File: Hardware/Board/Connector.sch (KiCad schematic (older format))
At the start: 76 parts, among them J10 WAGO_Klemmleiste_8-pol, J11 RJ12, J12 RJ45, J13 WAGO_Klemmleiste_6-pol, J16 Conn_01x06, J17 Conn_01x05, J18 WAGO_Klemmleiste_8-pol, J19 WAGO_Klemmleiste_8-pol, J2 Conn_02x25_Odd_Even, J20 Conn_02x03_Top_Bottom, J21 Conn_02x10_Odd_Even, J7 WAGO_Klemmleiste_6-pol, J8 WAGO_Klemmleiste_4-pol, J9 WAGO_Klemmleiste_8-pol, Q5 Q_NPN_BEC, Q6 Q_NPN_BEC

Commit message: Footprints zuweisungen
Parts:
- removed Q5, Q6: Q_NPN_BEC, symbol stmbl:Q_NPN_BEC
- added Q5, Q6: 2N7002, Package_TO_SOT_SMD:SOT-23, symbol Transistor_FET:2N7002
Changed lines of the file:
@@
-$EndComp
-$Comp
-L stmbl:Q_NPN_BEC Q6
-U 1 1 5D877437
-P 7800 2600
-F 0 "Q6" H 8000 3100 50  0000 L CNN
-F 1 "Q_NPN_BEC" H 7900 3000 50  0000 L CNN
-F 2 "" H 8000 2700 50  0001 C CNN
-F 3 "" H 7800 2600 50  0001 C CNN
-	1    7800 2600
-	-1   0    0    -1
-$EndComp
-$Comp
-L stmbl:Q_NPN_BEC Q5
-U 1 1 5D877543
-P 7450 2900
-F 0 "Q5" H 7700 3000 50  0000 L CNN
-F 1 "Q_NPN_BEC" H 7600 3150 50  0000 L CNN
-F 2 "" H 7650 3000 50  0001 C CNN
-F 3 "" H 7450 2900 50  0001 C CNN
-	1    7450 2900
-	-1   0    0    -1
 $EndComp
 $Comp
@@
 Wire Notes Line
 	5850 11100 5850 6700
+$Comp
+L Transistor_FET:2N7002 Q5
+U 1 1 5D1CDA94
+P 7450 2900
+F 0 "Q5" H 7656 2946 50  0000 L CNN
+F 1 "2N7002" H 7656 2855 50  0000 L CNN
+F 2 "Package_TO_SOT_SMD:SOT-23" H 7650 2825 50  0001 L CIN
+F 3 "https://www.fairchildsemi.com/datasheets/2N/2N7002.pdf" H 7450 2900 50  0001 L CNN
+	1    7450 2900
+	-1   0    0    -1
+$EndComp
+$Comp
+L Transistor_FET:2N7002 Q6
+U 1 1 5D1ED8DF
+P 7800 2600
+F 0 "Q6" H 8006 2646 50  0000 L CNN
+F 1 "2N7002" H 8006 2555 50  0000 L CNN
+F 2 "Package_TO_SOT_SMD:SOT-23" H 8000 2525 50  0001 L CIN
+F 3 "https://www.fairchildsemi.com/datasheets/2N/2N7002.pdf" H 7800 2600 50  0001 L CNN
+	1    7800 2600
+	-1   0    0    -1
+$EndComp
 $EndSCHEMATC

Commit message: Alle Footprints definiert, Libs angepasst, Layout gestartet mit Plazierung, Controller und Breakout Netzmäßig getrennt.
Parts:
- J16: footprint (none) -> SamacSys_Parts:436500628
- J17: footprint (none) -> SamacSys_Parts:436500527
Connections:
- net labels added: LCD_BL_CTR
- net labels removed: PA9
- wire segments 321 -> 320
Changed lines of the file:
@@
 Text GLabel 7800 9450 2    50   BiDi ~ 0
 PB2
-Text GLabel 7100 9450 0    50   BiDi ~ 0
-PA9
 Wire Wire Line
 	7100 7950 7200 7950
@@
 F 0 "J16" V 3450 8450 50  0000 L CNN
 F 1 "Conn_01x06" V 3350 8200 50  0000 L CNN
-F 2 "" H 3450 7850 50  0001 C CNN
+F 2 "SamacSys_Parts:436500628" H 3450 7850 50  0001 C CNN
 F 3 "~" H 3450 7850 50  0001 C CNN
 	1    3450 7850
@@
 F 0 "J17" V 3500 10150 50  0000 L CNN
 F 1 "Conn_01x05" V 3400 9850 50  0000 L CNN
-F 2 "" H 3450 9500 50  0001 C CNN
+F 2 "SamacSys_Parts:436500527" H 3450 9500 50  0001 C CNN
 F 3 "~" H 3450 9500 50  0001 C CNN
 	1    3450 9500
@@
 Text GLabel 4200 4950 0    50   BiDi ~ 0
 PC7
-Text GLabel 4200 5050 0    50   BiDi ~ 0
-PA9
 Text GLabel 4200 5150 0    50   BiDi ~ 0
 PB2
@@
 	4200 4950 4450 4950
 Connection ~ 4450 4950
-Wire Wire Line
-	4200 5050 4550 5050
-Connection ~ 4550 5050
 Wire Wire Line
 	4200 5150 4650 5150
@@
 	-1   0    0    -1
 $EndComp
+Text GLabel 7100 9450 0    50   Output ~ 0
+LCD_BL_CTR
 $EndSCHEMATC

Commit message: Komplete enummerierung Geändert, Schaltplan zusammengefasst, Layout nochmals reset. BOM zu 75% fertig gestellt
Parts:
- added C308: 47u, Capacitor_SMD:C_1210_3225Metric, symbol Device:C
- added C309, C310, C311, C312: 10u, Capacitor_SMD:C_1210_3225Metric, symbol Device:C
- added D300, D301, D302: B230, Diode_SMD:D_SMB, symbol Diode:B230
- added J314: SIM800-1, Connector_PinHeader_2.54mm:PinHeader_1x06_P2.54mm_Vertical, symbol Connector_Generic:Conn_01x06
- added J315: SIM800-2, Connector_PinSocket_2.54mm:PinSocket_1x06_P2.54mm_Vertical, symbol Connector_Generic:Conn_01x06
- added J316: Raspberry_Pi_2_3, Connector_IDC:IDC-Header_2x20_P2.54mm_Vertical, symbol Connector:Raspberry_Pi_2_3
- added U300: ESP-12F, RF_Module:ESP-12E, symbol RF_Module:ESP-12F
- J300: renamed from J8; value WAGO_Klemmleiste_4-pol -> Power In
- J301: renamed from J9; value WAGO_Klemmleiste_8-pol -> 1Wire 1-4
- J302: renamed from J10; value WAGO_Klemmleiste_8-pol -> 1Wire 5-8
- J303: renamed from J7; value WAGO_Klemmleiste_6-pol -> LIN 1-3
- J304: renamed from J11; value RJ12 -> Truma
- J305: renamed from J12; value RJ45 -> Dormetic
- J306: renamed from J18; value WAGO_Klemmleiste_8-pol -> Analog 1-4
- J307: renamed from J19; value WAGO_Klemmleiste_8-pol -> Analog 5-8
- J308: renamed from J16; value Conn_01x06 -> Wasser
- J309: renamed from J17; value Conn_01x05 -> Abwasser
- J310: renamed from J13; value WAGO_Klemmleiste_6-pol -> CAN + RS485
- J311: renamed from J20; value Conn_02x03_Top_Bottom -> Schaudt EBL
- J312: renamed from J21; value Conn_02x10_Odd_Even -> Spare
- J313: renamed from J2; value Conn_02x25_Odd_Even -> CPU
- renumbered C89 to C300, C91 to C301, C93 to C302, C95 to C303, C90 to C304, C92 to C305, C94 to C306, C96 to C307, D16 to D303, D17 to D304, D18 to D305, FB18 to FB300, FB19 to FB301, FB20 to FB302, FB21 to FB303, FB22 to FB304, FB23 to FB305, FB24 to FB306, FB25 to FB307, FB26 to FB308, FB35 to FB309, FB36 to FB310, FB37 to FB311, FB27 to FB312, FB29 to FB313, FB31 to FB314, FB33 to FB315, FB28 to FB316, FB30 to FB317, FB32 to FB318, FB34 to FB319, FB42 to FB320, FB40 to FB321, FB38 to FB322, FB44 to FB323, FB43 to FB324, FB41 to FB325, FB39 to FB326, Q6 to Q300, Q5 to Q301, R53 to R300, R55 to R301, R57 to R302, R59 to R303, R61 to R304, R62 to R305, R63 to R306, R64 to R307, R54 to R308, R56 to R309, R58 to R310, R60 to R311, R65 to R312, R66 to R313, R67 to R314, R68 to R315, R70 to R316, R69 to R317, R71 to R318, R72 to R319, R73 to R320, R74 to R321
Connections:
- net labels added: +4V, +5VD
- wire segments 320 -> 374
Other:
- note added: "SIM800L Modul\n"

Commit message: Änderung des Konzeptes auf 2 Boards, eines TFT Touch mit STM32L4R9, das rein die Bedienung macht. Control Board mit STM32L476, mit noch mehr Schnittstellen. Bus zwischen Display, Board, Raspberry/ESP ist RS485, Bus als RJ45 mit Wakeup und Stromversorgung
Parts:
- removed J313: CPU, Connector_PinSocket_2.54mm:PinSocket_2x25_P2.54mm_Vertical, symbol Connector_Generic:Conn_02x25_Odd_Even
- added C?: 100nF, Capacitor_SMD:C_0603_1608Metric, symbol Device:C
- added D?: NUP2105L, Package_TO_SOT_SMD:SOT-23, symbol Device:D_TVS_x2_AAC
- added FB? (x2): 100R, Inductor_SMD:L_0603_1608Metric, symbol Device:Ferrite_Bead_Small
- added R?: 120R, Resistor_SMD:R_0603_1608Metric, symbol Device:R
- added R? (x2): 10R, Resistor_SMD:R_0603_1608Metric, symbol Device:R
- added U?: MAX3072E, Package_SO:SOIC-8_3.9x4.9mm_P1.27mm, symbol Interface_UART:MAX3072E
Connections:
- net labels added: CTRL_A, CTRL_B, CTRL_BUS_A, CTRL_BUS_B, RASPI_RTS_DE_CTRL, RASPI_RX_CTRL, RASPI_TX_CTRL
- net labels removed: CAN1_RX, CAN1_TX, I2C2_SCL, I2C2_SDA, LCD_BL_CTR, LCD_LED-A, LCD_LED-K, LPUART_RTS_DE_RS485, LPUART_RX_RX485, LPUART_TX_RS485, PWR_Reset, USART1_RX_LIN1, USART1_TX_LIN1, USART2_RX_LIN2, USART2_TX_LIN2, USART3_RX_LIN3, USART3_TX_LIN3
- wire segments 374 -> 348

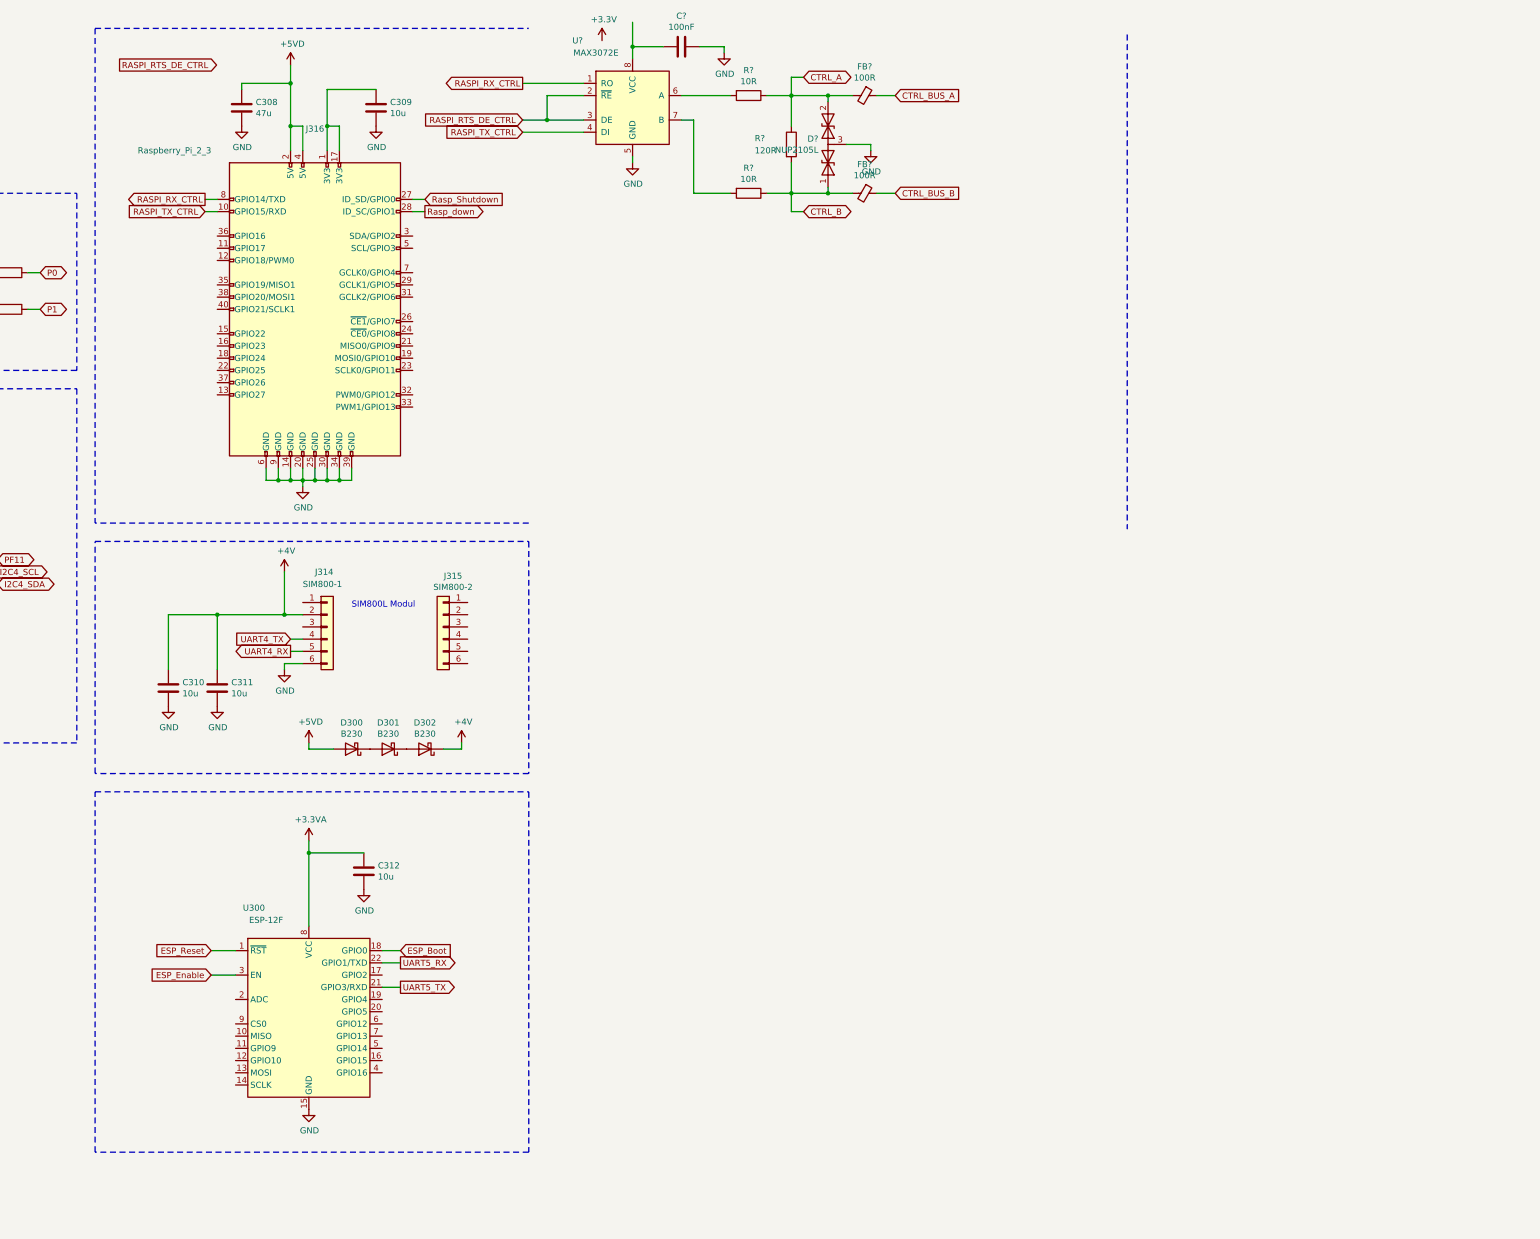
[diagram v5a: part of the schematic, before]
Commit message: Display Unit Lib Fehler behoben, und noch Zeug raus geworfen Library jetzt projekt spezifisch im Hardware root.. Hauptplatine rund um den Prozessor a bissl was getan, vorbereitung Quadspi Flash und SD Karte.
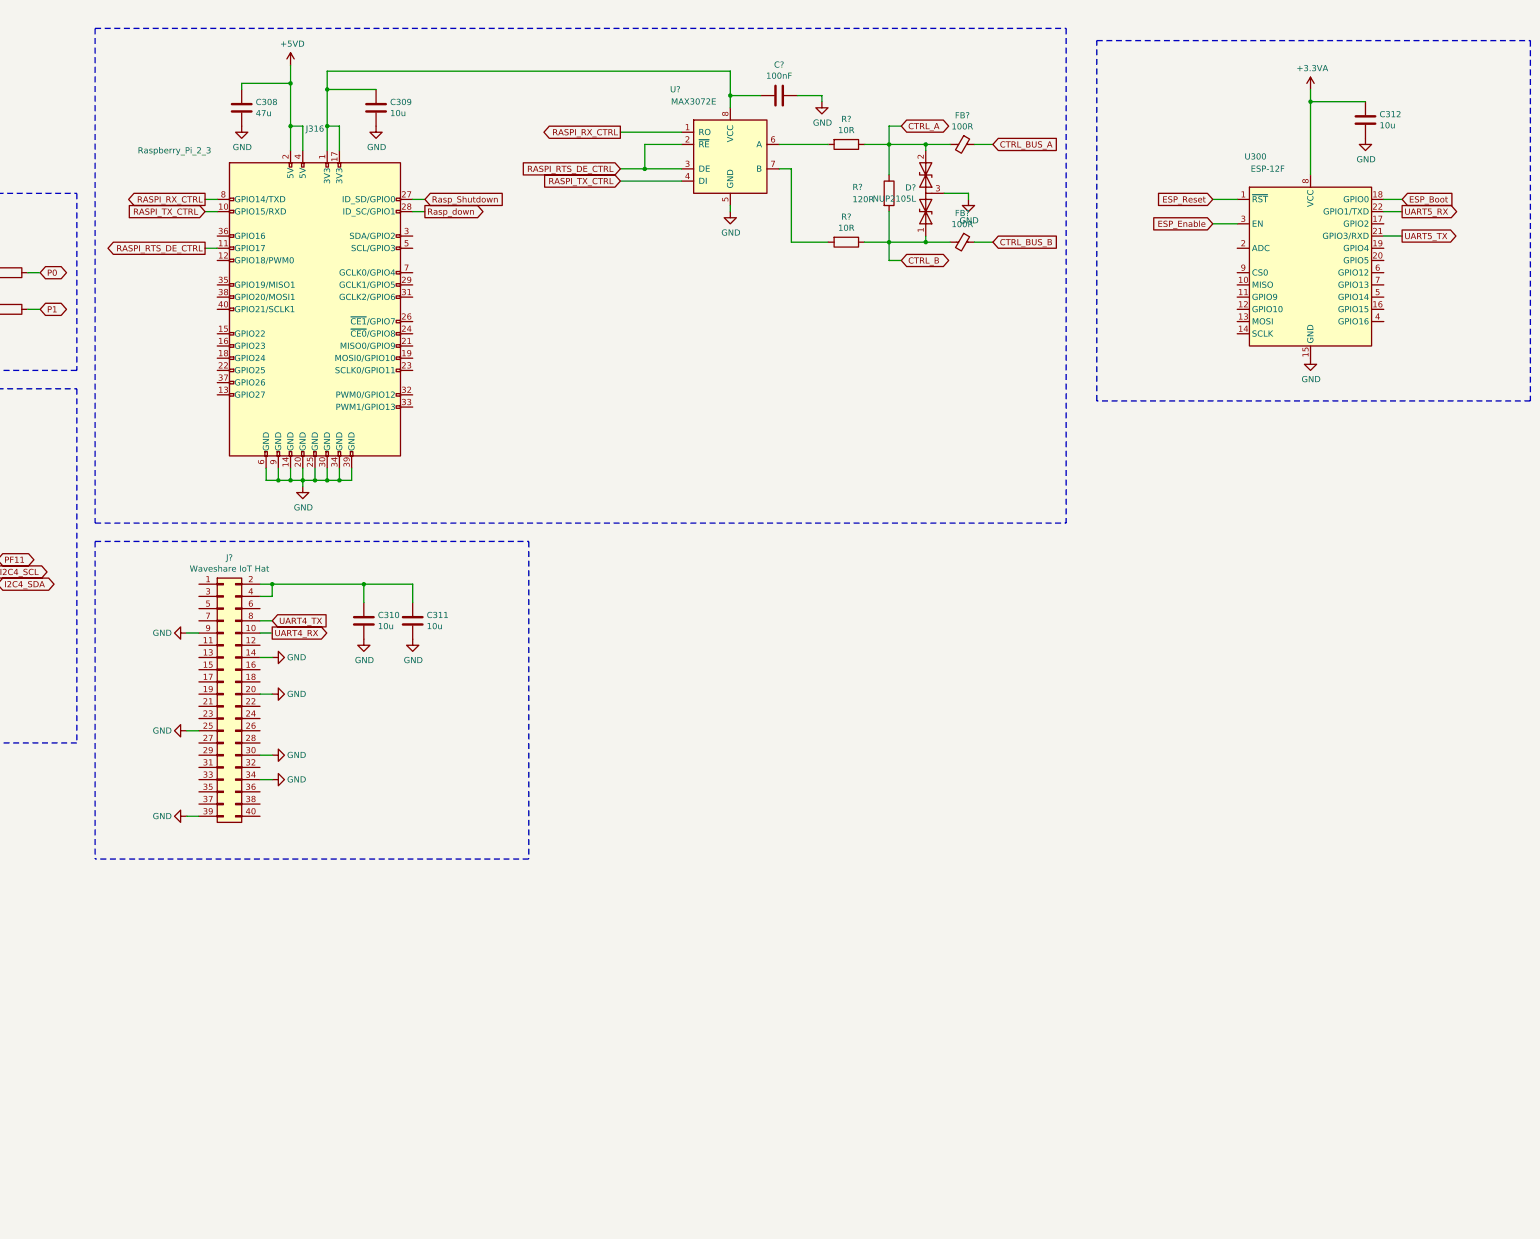
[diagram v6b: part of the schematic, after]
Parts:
- removed D300, D301, D302: B230, Diode_SMD:D_SMB, symbol Diode:B230
- removed J314: SIM800-1, Connector_PinHeader_2.54mm:PinHeader_1x06_P2.54mm_Vertical, symbol Connector_Generic:Conn_01x06
- removed J315: SIM800-2, Connector_PinSocket_2.54mm:PinSocket_1x06_P2.54mm_Vertical, symbol Connector_Generic:Conn_01x06
- added J?: Waveshare IoT Hat, symbol Connector_Generic:Conn_02x20_Odd_Even
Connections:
- net GND: now also J?.14 (Pin_14), J?.20 (Pin_20), J?.25 (Pin_25), J?.30 (Pin_30), J?.34 (Pin_34), J?.39 (Pin_39), J?.9 (Pin_9)
- net RASPI_RTS_DE_CTRL: now also J316.11 (GPIO17)
- net UART4_RX: now also J?.10 (Pin_10)
- net UART4_TX: now also J?.8 (Pin_8)
- net at C309.1, J316.1 (3V3), J316.17 (3V3): now also C?.2, U?.8 (VCC)
- net +4V: no longer names the net of C310.1, C311.1
- net +4V: now also J?.2 (Pin_2), J?.4 (Pin_4)
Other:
- note removed: "SIM800L Modul\n"
- moved on the sheet: C310, C311, C312, C?, D?, FB?, R?, U300, U?

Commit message: Alle Busse aus dem Prozessor geroutet, Multplexing der LIN, RS485 und TTY Busse, diverse Aufräumarbeiten.
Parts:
- removed C?: 100nF, Capacitor_SMD:C_0603_1608Metric, symbol Device:C
- removed D?: NUP2105L, Package_TO_SOT_SMD:SOT-23, symbol Device:D_TVS_x2_AAC
- removed FB? (x2): 100R, Inductor_SMD:L_0603_1608Metric, symbol Device:Ferrite_Bead_Small
- removed R?: 120R, Resistor_SMD:R_0603_1608Metric, symbol Device:R
- removed R? (x2): 10R, Resistor_SMD:R_0603_1608Metric, symbol Device:R
- removed U?: MAX3072E, Package_SO:SOIC-8_3.9x4.9mm_P1.27mm, symbol Interface_UART:MAX3072E
- added C? (x2): 100nF, Capacitor_SMD:C_0603_1608Metric, symbol Device:C
- added C?: 5n6, Capacitor_SMD:C_0603_1608Metric, symbol Device:C
- added D?: NUP2105L, Package_TO_SOT_SMD:SOT-23, symbol Device:D_TVS_x2_AAC
- added FB? (x2): 100R, Inductor_SMD:L_0603_1608Metric, symbol Device:Ferrite_Bead_Small
- added R? (x2): 60R, Resistor_SMD:R_0603_1608Metric, symbol Device:R
- added U?: TJA1049T-3, Package_SO:SOIC-8_3.9x4.9mm_P1.27mm, symbol Interface_CAN_LIN:TJA1049T-3
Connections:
- net +5VD: now also C?.2, U?.3 (VCC)
- net GND: now also C?.1, C?.2, C?.2, D?.3 (common), U?.2 (GND)
- net RASPI_RX_CTRL: now also U?.4 (RXD)
- net RASPI_TX_CTRL: now also U?.1 (TXD)
- net at C309.1, J316.1 (3V3), J316.17 (3V3): now also C?.1, U?.5 (VIO)
- net +5VL: now reaches C310.1, C311.1, J?.2 (Pin_2), J?.4 (Pin_4)
- net RASPI_RTS_DE_CTRL renamed STB_RASPI_CTRL
- net UART4_RX renamed UART4_RX_GSM
- net UART4_TX renamed UART4_TX_GSM
- new net: C?.1, R?.1, R?.2
- new net CTRL_BUS_H: FB?.1
- new net CTRL_BUS_L: FB?.1
- new net CTRL_H: D?.2 (A2), FB?.2, R?.1, U?.7 (CANH)
- new net CTRL_L: D?.1 (A1), FB?.2, R?.2, U?.6 (CANL)
- new net STB-RASPI_CTRL: U?.8 (STB)

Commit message: Prozessor Pins zugeordnet, 4 bistabile Relais, CAN Control Interface, CAN Debug Adapter, Lagesensor zugefügt, Umwelt Sensor, ISM 868 MHz Tranceiver, ESP and Control Bus. UID Eprom. Etliche Aufräum Arbeiten.
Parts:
- added C?: 5n6, Capacitor_SMD:C_0603_1608Metric, symbol Device:C
- added C?: 4u7, Capacitor_SMD:C_0603_1608Metric, symbol Device:C
- added C? (x10): 100nF, Capacitor_SMD:C_0603_1608Metric, symbol Device:C
- added C?: 220nF, Capacitor_SMD:C_0603_1608Metric, symbol Device:C
- added C?: 10uF, Capacitor_SMD:C_0603_1608Metric, symbol Device:C
- added D? (x4): BAV70, Package_TO_SOT_SMD:SOT-23, symbol Diode:BAV70
- added D?: NUP2105L, Package_TO_SOT_SMD:SOT-23, symbol Device:D_TVS_x2_AAC
- added D?: SP0504BAJT, Package_TO_SOT_SMD:SOT-353_SC-70-5, symbol Power_Protection:SP0504BAJT
- added FB? (x8): 100R, Inductor_SMD:L_0603_1608Metric, symbol Device:Ferrite_Bead_Small
- added J? (x2): RJ45_Shielded, symbol Connector:RJ45_Shielded
- added J?: USB_B_Micro, Connector_USB:USB_Micro-B_Molex-105017-0001, symbol Connector:USB_B_Micro
- added J? (x2): SENSOR, symbol Connector_Generic:Conn_02x05_Odd_Even
- added K? (x4): 5-1393243-2, 513932432, symbol Womo-Lin:5-1393243-2
- added R? (x4): 47K, Resistor_SMD:R_0603_1608Metric, symbol Device:R
- added R? (x2): 60R, Resistor_SMD:R_0603_1608Metric, symbol Device:R
- added R? (x2): 10K, Resistor_SMD:R_0603_1608Metric, symbol Device:R
- added U? (x2): TJA1049T-3, Package_SO:SOIC-8_3.9x4.9mm_P1.27mm, symbol Interface_CAN_LIN:TJA1049T-3
- added U?: FT232RL, Package_SO:SSOP-28_5.3x10.2mm_P0.65mm, symbol Interface_USB:FT232RL
- added U?: USBLC6-2SC6, Package_TO_SOT_SMD:SOT-23-6, symbol Power_Protection:USBLC6-2SC6
- added U?: LSM303AGR, symbol Sensor_Motion:LSM303C
- added U?: BME680, Package_LGA:Bosch_LGA-8_3x3mm_P0.8mm_ClockwisePinNumbering, symbol Sensor:BME680
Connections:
- net +3.3VA: now also C?.1, C?.1, C?.1, C?.1, C?.1, C?.1, J?.2 (Pin_2), J?.2 (Pin_2), J?.4 (Pin_4), J?.4 (Pin_4), R?.1, R?.1, R?.2, R?.2, R?.2, R?.2, U?.10 (VDDIO), U?.2 (CSB), U?.2 (CS_XL), U?.3 (CS_MAG), U?.5 (VIO), U?.6 (VDDIO), U?.8 (VDD), U?.9 (VDD)
- net +5V: now also D?.3 (K), D?.3 (K), D?.3 (K), D?.3 (K), K?.A3 (+), K?.A3 (+), K?.A3 (+), K?.A3 (+)
- net +5VD: now also C?.2, U?.3 (VCC)
- net +BATT: now also J?.1, J?.2
- net CTRL_BUS_H: now also FB?.1, J?.4, J?.4
- net CTRL_BUS_L: now also FB?.1, J?.5, J?.5
- net CTRL_H: now also U?.7 (CANH)
- net CTRL_L: now also U?.6 (CANL)
- net GND: now also C?.1, C?.1, C?.2, C?.2, C?.2, C?.2, C?.2, C?.2, C?.2, C?.2, C?.2, C?.2, C?.2, C?.2, D?.2 (A), D?.3 (common), J?.10 (Pin_10), J?.10 (Pin_10), J?.5 (GND), J?.6 (Pin_6), J?.6 (Pin_6), J?.6 (Shield), J?.7, J?.7, J?.8, J?.8, J?.8 (Pin_8), J?.8 (Pin_8), J?.SH, J?.SH, K?.22 (NC_2), K?.22 (NC_2), K?.22 (NC_2), K?.22 (NC_2), U?.1 (GND), U?.18 (GND), U?.2 (GND), U?.2 (GND), U?.2 (GND), U?.21 (GND), U?.25 (AGND), U?.5 (SDO), U?.6 (GND), U?.7 (GND), U?.7 (GND), U?.8 (GND), U?.8 (STB)
- net at U300.17 (GPIO2): now also U?.8 (STB)
- net I2C4_SCL: no longer names the net of D305.3 (K), FB325.2
- net I2C4_SDA: no longer names the net of D305.1 (K), FB326.2
- net PF11: no longer names the net of D305.4 (K), FB324.2
- net UART5_RX: no longer names the net of U300.22 (GPIO1/TXD)
- net UART5_RX: now also U?.1 (TXD)
- net UART5_TX: no longer names the net of U300.21 (GPIO3/RXD)
- net UART5_TX: now also U?.4 (RXD)
- new net: U?.1 (TXD), U?.1 (TXD)
- new net: C?.1, C?.1, C?.1, FB?.2, U?.20 (VCC), U?.3 (VCC), U?.4 (VCCIO), U?.5 (VIO)
- new net: U?.4 (RXD), U?.5 (RXD)
- new net: D?.1 (A1), FB?.2, R?.2, U?.6 (CANL)
- new net: D?.2 (A2), FB?.2, R?.1, U?.7 (CANH)
- new net: C?.1, R?.1, R?.2
- new net: U?.15 (USBD+), U?.3 (IO2)
- new net: U?.1 (IO1), U?.16 (USBD-)
- new net: C?.2, U?.17 (3V3OUT)
- new net: C?.1, FB?.1, J?.1 (VBUS), U?.5 (VBUS)
- new net: J?.2 (D-), U?.6 (IO1)
- new net: J?.3 (D+), U?.4 (IO2)
- new net: C?.1, U?.5 (C1)
- new net: FB?.2, J?.1 (Pin_1)
- new net: FB?.2, J?.3 (Pin_3)
- new net: FB?.2, J?.5 (Pin_5)
- new net: FB?.2, J?.7 (Pin_7)
- new net: FB?.2, J?.9 (Pin_9)
- new net I2C3_SCL: J?.7 (Pin_7), R?.2, U?.1 (SCL/SPC), U?.4 (SCK)
- new net I2C3_SDA: J?.9 (Pin_9), R?.2, U?.3 (SDI), U?.4 (SDA/SDI/SDO)
- new net INT_1_XL: J?.5 (Pin_5), U?.12 (INT_XL)
- new net INT_MAG_DRDY: J?.3 (Pin_3), U?.7 (INT_MAG)
- new net INt_2_XL: J?.1 (Pin_1), U?.11 (DRDY_MAG)
- new net K1_COM: K?.11 (COM_1)
- new net K1_NC: K?.12 (NC_1)
- new net K1_NO: K?.14 (NO_1)
- new net K1_RESET: D?.2 (A), K?.A1 (Reset)
- new net K1_SET: D?.1 (A), K?.A2 (Set)
- new net K1_STATUS: K?.21 (COM_2), R?.1
- new net K2_COM: K?.11 (COM_1)
- new net K2_NC: K?.12 (NC_1)
- new net K2_NO: K?.14 (NO_1)
- new net K2_RESET: D?.2 (A), K?.A1 (Reset)
- new net K2_SET: D?.1 (A), K?.A2 (Set)
- new net K2_STATUS: K?.21 (COM_2), R?.1
- new net K3_COM: K?.11 (COM_1)
- new net K3_NC: K?.12 (NC_1)
- new net K3_NO: K?.14 (NO_1)
- new net K3_RESET: D?.2 (A), K?.A1 (Reset)
- new net K3_SET: D?.1 (A), K?.A2 (Set)
- new net K3_STATUS: K?.21 (COM_2), R?.1
- new net K4_COM: K?.11 (COM_1)
- new net K4_NC: K?.12 (NC_1)
- new net K4_NO: K?.14 (NO_1)
- new net K4_RESET: D?.2 (A), K?.A1 (Reset)
- new net K4_SET: D?.1 (A), K?.A2 (Set)
- new net K4_STATUS: K?.21 (COM_2), R?.1
- no-connect marks 0 -> 14
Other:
- note added: "ACL I2C-ADR: 0011001"
- note added: "Control Bus Debug Adapter\nBoard section is breakable for seperate use"
- note added: "I2C-ADR: 1110110"
- note added: "MAG I2C-ADR: 0011110"
- note added: "MAG, ACL, Enviroment Sensors\nThis have ben mount horizontaly and in\nAir Flow, can be seperatd from main board\nUse 10 Pin 1:1 Ribbon cable instat"
